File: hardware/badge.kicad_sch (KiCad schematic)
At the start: 53 parts, among them J1 SAO V.1.69bis master, Q1 BSS138, SW1 power, SW2 SW_Push, SW3 update epaper, U1 Seeed XIAO ESP32-C3, U2 MH-ET_epaper_ 2.13, U3 5V boost converter, U4 TXS0104EPWR

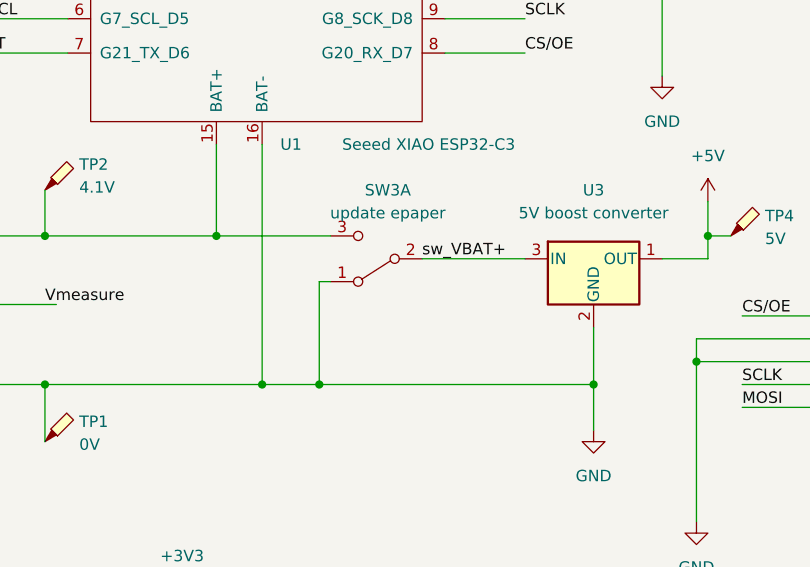
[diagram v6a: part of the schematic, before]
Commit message: add diode to ensure boost converter Vin < Vo
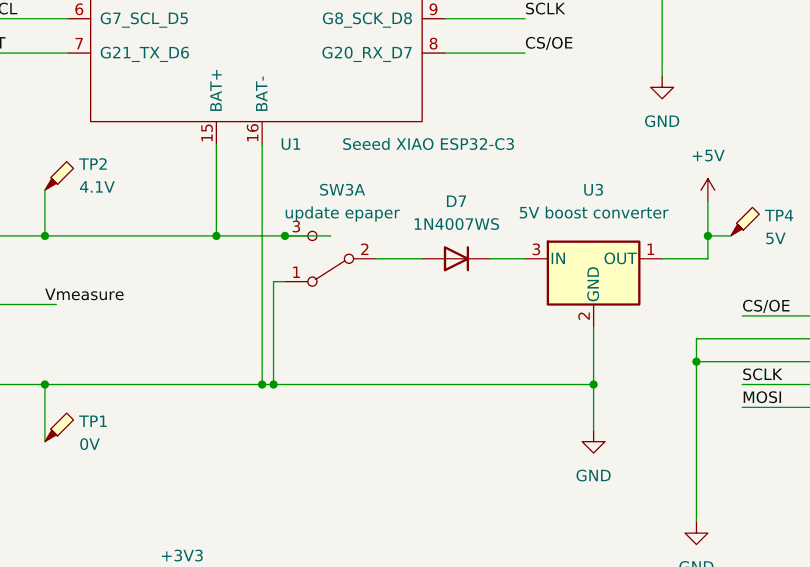
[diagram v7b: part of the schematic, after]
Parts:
- added D7: 1N4007WS, Diode_SMD:D_SOD-323_HandSoldering, symbol Device:D
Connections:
- net sw_VBAT+: no longer names the net of U3.3 (IN)
- net sw_VBAT+: now also D7.1 (K); no longer SW3.2 (B)
- new net: D7.2 (A), SW3.2 (B)
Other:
- moved on the sheet: SW3A
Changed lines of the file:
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@@
 	)
 	(junction
-		(at 104.14 97.79)
+		(at 99.06 97.79)
 		(diameter 0)
 		(color 0 0 0 0)
@@
 	)
 	(junction
+		(at 100.33 81.28)
+		(diameter 0)
+		(color 0 0 0 0)
+	)
+	(junction
 		(at 224.79 113.03)
 		(diameter 0)
@@
 	(wire
 		(pts
+			(xy 100.33 81.28) (xy 105.41 81.28)
+		)
+		(stroke
+			(width 0)
+			(type default)
+		)
+	)
+	(wire
+		(pts
 			(xy 243.84 57.15) (xy 220.98 57.15)
 		)
@@
 	(wire
 		(pts
+			(xy 110.49 83.82) (xy 115.57 83.82)
+		)
+		(stroke
+			(width 0)
+			(type default)
+		)
+	)
+	(wire
+		(pts
 			(xy 252.73 81.28) (xy 267.97 81.28)
 		)
@@
 	(wire
 		(pts
-			(xy 104.14 97.79) (xy 134.62 97.79)
-		)
-		(stroke
-			(width 0)
-			(type default)
-		)
-	)
-	(wire
-		(pts
 			(xy 224.79 113.03) (xy 236.22 113.03)
 		)
@@
 	(wire
 		(pts
-			(xy 105.41 86.36) (xy 104.14 86.36)
+			(xy 100.33 86.36) (xy 99.06 86.36)
 		)
 		(stroke
@@
 	(wire
 		(pts
-			(xy 92.71 81.28) (xy 105.41 81.28)
+			(xy 92.71 81.28) (xy 100.33 81.28)
 		)
 		(stroke
@@
 	(wire
 		(pts
+			(xy 99.06 97.79) (xy 134.62 97.79)
+		)
+		(stroke
+			(width 0)
+			(type default)
+		)
+	)
+	(wire
+		(pts
 			(xy 97.79 71.12) (xy 97.79 97.79)
 		)
@@
 	(wire
 		(pts
-			(xy 104.14 86.36) (xy 104.14 97.79)
+			(xy 99.06 86.36) (xy 99.06 97.79)
 		)
 		(stroke
@@
 	(wire
 		(pts
+			(xy 123.19 83.82) (xy 127 83.82)
+		)
+		(stroke
+			(width 0)
+			(type default)
+		)
+	)
+	(wire
+		(pts
 			(xy 238.76 35.56) (xy 238.76 49.53)
 		)
@@
 	(wire
 		(pts
-			(xy 97.79 97.79) (xy 104.14 97.79)
+			(xy 97.79 97.79) (xy 99.06 97.79)
 		)
 		(stroke
@@
 	(wire
 		(pts
-			(xy 115.57 83.82) (xy 127 83.82)
-		)
-		(stroke
-			(width 0)
-			(type default)
-		)
-	)
-	(wire
-		(pts
 			(xy 257.81 135.89) (xy 266.7 135.89)
 		)
@@
 		)
 	)
-	(label "sw_VBAT+"
-		(at 115.57 83.82 0)
-		(fields_autoplaced yes)
-		(effects
-			(font
-				(size 1.27 1.27)
-			)
-			(justify left bottom)
-		)
-	)
 	(label "ls_MOSI"
 		(at 187.96 86.36 0)
@@
 	)
 	(symbol
+		(lib_id "Device:D")
+		(at 119.38 83.82 180)
+		(unit 1)
+		(exclude_from_sim no)
+		(in_bom yes)
+		(on_board yes)
+		(dnp no)
+		(fields_autoplaced yes)
+		(property "Reference" "D7"
+			(at 119.38 77.47 0)
+			(effects
+				(font
+					(size 1.27 1.27)
+				)
+			)
+		)
+		(property "Value" "1N4007WS"
+			(at 119.38 80.01 0)
+			(effects
+				(font
+					(size 1.27 1.27)
+				)
+			)
+		)
+		(property "Footprint" "Diode_SMD:D_SOD-323_HandSoldering"
+			(at 119.38 83.82 0)
+			(effects
+				(font
+					(size 1.27 1.27)
+				)
+				(hide yes)
+			)
+		)
+		(property "Datasheet" "https://datasheet.lcsc.com/lcsc/2201251830_YFW-1N4007WS_C2898417.pdf"
+			(at 119.38 83.82 0)
+			(effects
+				(font
+					(size 1.27 1.27)
+				)
+				(hide yes)
+			)
+		)
+		(property "Description" "Diode"
+			(at 119.38 83.82 0)
+			(effects
+				(font
+					(size 1.27 1.27)
+				)
+				(hide yes)
+			)
+		)
+		(property "Sim.Device" "D"
+			(at 119.38 83.82 0)
+			(effects
+				(font
+					(size 1.27 1.27)
+				)
+				(hide yes)
+			)
+		)
+		(property "Sim.Pins" "1=K 2=A"
+			(at 119.38 83.82 0)
+			(effects
+				(font
+					(size 1.27 1.27)
+				)
+				(hide yes)
+			)
+		)
+		(pin "2"
+		)
+		(pin "1"
+		)
+		(instances
+			(project "badge"
+				(path "/86e9ced6-67f5-4007-880a-280020fc259e"
+					(reference "D7")
+					(unit 1)
+				)
+			)
+		)
+	)
+	(symbol
 		(lib_id "Connector:TestPoint_Probe")
 		(at 73.66 76.2 0)
@@
 	(symbol
 		(lib_id "Switch:SW_DPDT_x2")
-		(at 110.49 83.82 180)
+		(at 105.41 83.82 180)
 		(unit 1)
 		(exclude_from_sim no)
@@
 		(dnp no)
 		(property "Reference" "SW3"
-			(at 111.76 76.2 0)
+			(at 106.68 76.2 0)
 			(effects
 				(font
@@
 		)
 		(property "Value" "update epaper"
-			(at 111.76 78.74 0)
+			(at 106.68 78.74 0)
 			(effects
 				(font
@@
 		)
 		(property "Footprint" "extra:MSS-22D18G2 hand-solderable"
-			(at 110.49 83.82 0)
+			(at 105.41 83.82 0)
 			(effects
 				(font
@@
 		)
 		(property "Datasheet" "~"
-			(at 110.49 83.82 0)
+			(at 105.41 83.82 0)
 			(effects
 				(font
@@
 		)
 		(property "Description" ""
-			(at 110.49 83.82 0)
+			(at 105.41 83.82 0)
 			(effects
 				(font

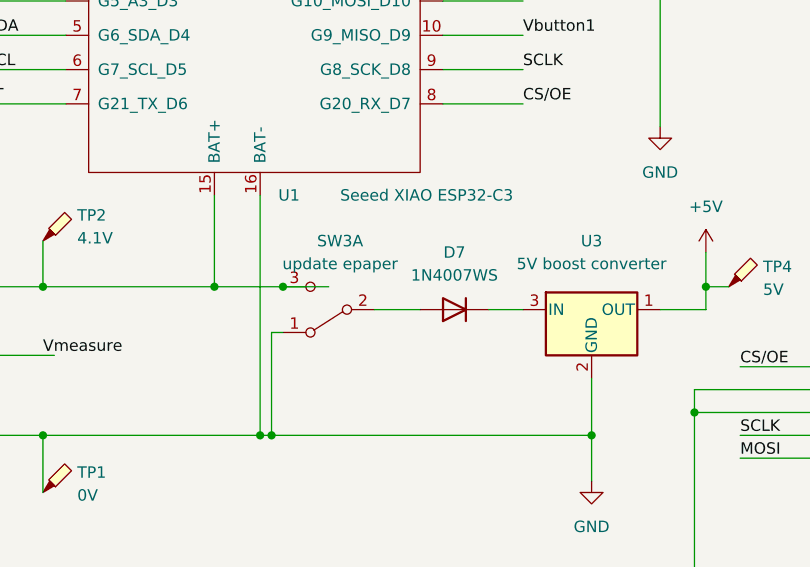
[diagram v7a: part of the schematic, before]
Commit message: change to higher-rated diode
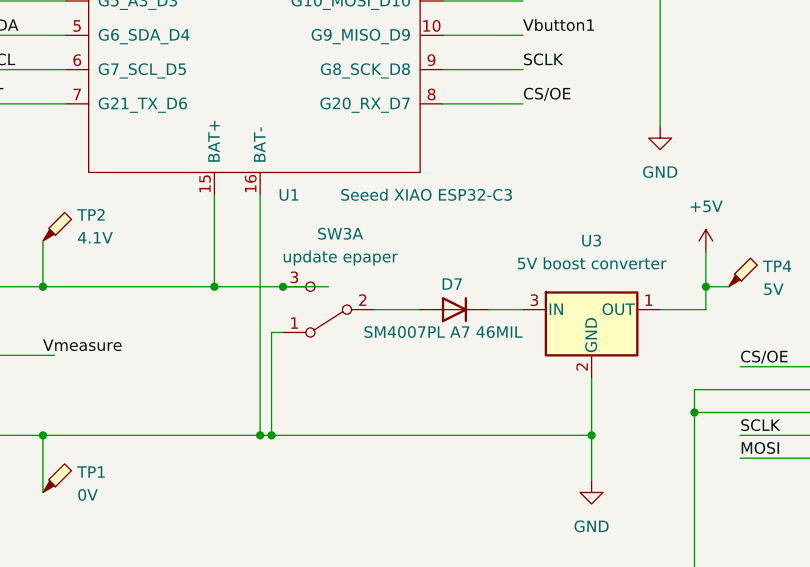
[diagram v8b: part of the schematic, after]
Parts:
- D7: value 1N4007WS -> SM4007PL A7 46MIL; footprint Diode_SMD:D_SOD-323_HandSoldering -> Diode_SMD:D_SOD-123F
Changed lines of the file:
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@@
 		(on_board yes)
 		(dnp no)
-		(fields_autoplaced yes)
 		(property "Reference" "D7"
-			(at 119.38 77.47 0)
-			(effects
-				(font
-					(size 1.27 1.27)
-				)
-			)
-		)
-		(property "Value" "1N4007WS"
-			(at 119.38 80.01 0)
-			(effects
-				(font
-					(size 1.27 1.27)
-				)
-			)
-		)
-		(property "Footprint" "Diode_SMD:D_SOD-323_HandSoldering"
-			(at 119.38 83.82 0)
-			(effects
-				(font
-					(size 1.27 1.27)
-				)
-				(hide yes)
-			)
-		)
-		(property "Datasheet" "https://datasheet.lcsc.com/lcsc/2201251830_YFW-1N4007WS_C2898417.pdf"
+			(at 119.126 81.026 0)
+			(effects
+				(font
+					(size 1.27 1.27)
+				)
+			)
+		)
+		(property "Value" "SM4007PL A7 46MIL"
+			(at 118.11 86.36 0)
+			(effects
+				(font
+					(size 1.27 1.27)
+				)
+			)
+		)
+		(property "Footprint" "Diode_SMD:D_SOD-123F"
+			(at 119.38 83.82 0)
+			(effects
+				(font
+					(size 1.27 1.27)
+				)
+				(hide yes)
+			)
+		)
+		(property "Datasheet" "https://datasheet.lcsc.com/lcsc/2111101130_YONGYUTAI-SM4007PL-A7-46MIL_C2916249.pdf"
 			(at 119.38 83.82 0)
 			(effects
@@
 		(dnp no)
 		(property "Reference" "SW3"
-			(at 106.68 76.2 0)
+			(at 106.68 75.438 0)
 			(effects
 				(font
@@
 		)
 		(property "Value" "update epaper"
-			(at 106.68 78.74 0)
-			(effects
-				(font
+			(at 106.68 77.978 0)
+			(effects
+				(font
